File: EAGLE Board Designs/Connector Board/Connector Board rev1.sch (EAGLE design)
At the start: 39 parts, among them J1 CONNECTOR-8_μF_T_V_BLACK, J10 CONNECTOR-16_MF_T_V_, J11 CONNECTOR-18_MF_T_V_, J12 CONNECTOR-8_μF_T_V_BLACK, J2 CONNECTOR-8_μF_T_V_BLACK, J3 CONNECTOR-8_μF_T_V_BLACK, J4 CONNECTOR-10_MF_T_V_, J5 CONNECTOR-4_μF_T_V_BLACK, J6 CONNECTOR-34__, J7 CONNECTOR-34__, J8 CONNECTOR-4_μF_T_V_BLACK, J9 CONNECTOR-4_μF_T_V_BLACK, Q1 TRANSISTOR_N_MOS__DMG3406L-7, Q2 TRANSISTOR_P_MOS_SOT-23_DMP30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, Q3 TRANSISTOR_N_MOS__DMG3406L-7, Q4 TRANSISTOR_P_MOS_SOT-23_DMP30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, Q5 TRANSISTOR_N_MOS__DMG3406L-7, Q6 TRANSISTOR_P_MOS_SOT-23_DMP30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

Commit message: added CAN test points
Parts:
- added TP1, TP2, TP3, TP4, TP5, TP6: TEST_POINT, HyTechDevices:TEST_POINT
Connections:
- net CANH_1: now also TP3.1
- net CANH_2: now also TP1.1
- net CANH_3: now also TP6.1
- net CANL_1: now also TP4.1
- net CANL_2: now also TP2.1
- net CANL_3: now also TP5.1
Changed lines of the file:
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@@
 <part name="R2" library="HyTechDevices" deviceset="RESISTOR_?_*" device="0603" technology="100"/>
 <part name="R3" library="HyTechDevices" deviceset="RESISTOR_?_*" device="0603" technology="100"/>
+<part name="TP1" library="HyTechDevices" deviceset="TEST_POINT" device=""/>
+<part name="TP2" library="HyTechDevices" deviceset="TEST_POINT" device=""/>
+<part name="TP3" library="HyTechDevices" deviceset="TEST_POINT" device=""/>
+<part name="TP4" library="HyTechDevices" deviceset="TEST_POINT" device=""/>
+<part name="TP5" library="HyTechDevices" deviceset="TEST_POINT" device=""/>
+<part name="TP6" library="HyTechDevices" deviceset="TEST_POINT" device=""/>
 </parts>
 <sheets>
@@
 <attribute name="RESISTANCE" x="102.87" y="184.15" size="1.27" layer="96" align="top-center"/>
 </instance>
+<instance part="TP1" gate="G$1" x="254" y="198.12" smashed="yes" rot="R180">
+<attribute name="NAME" x="256.54" y="196.342" size="1.27" layer="95" rot="R180"/>
+<attribute name="MPN" x="256.54" y="199.898" size="1.27" layer="95" rot="R180" align="top-left"/>
+</instance>
+<instance part="TP2" gate="G$1" x="261.62" y="195.58" smashed="yes" rot="R180">
+<attribute name="NAME" x="264.16" y="193.802" size="1.27" layer="95" rot="R180"/>
+<attribute name="MPN" x="264.16" y="197.358" size="1.27" layer="95" rot="R180" align="top-left"/>
+</instance>
+<instance part="TP3" gate="G$1" x="269.24" y="193.04" smashed="yes" rot="R180">
+<attribute name="NAME" x="271.78" y="191.262" size="1.27" layer="95" rot="R180"/>
+<attribute name="MPN" x="271.78" y="194.818" size="1.27" layer="95" rot="R180" align="top-left"/>
+</instance>
+<instance part="TP4" gate="G$1" x="254" y="190.5" smashed="yes" rot="R180">
+<attribute name="NAME" x="256.54" y="188.722" size="1.27" layer="95" rot="R180"/>
+<attribute name="MPN" x="256.54" y="192.278" size="1.27" layer="95" rot="R180" align="top-left"/>
+</instance>
+<instance part="TP5" gate="G$1" x="261.62" y="187.96" smashed="yes" rot="R180">
+<attribute name="NAME" x="264.16" y="186.182" size="1.27" layer="95" rot="R180"/>
+<attribute name="MPN" x="264.16" y="189.738" size="1.27" layer="95" rot="R180" align="top-left"/>
+</instance>
+<instance part="TP6" gate="G$1" x="269.24" y="185.42" smashed="yes" rot="R180">
+<attribute name="NAME" x="271.78" y="183.642" size="1.27" layer="95" rot="R180"/>
+<attribute name="MPN" x="271.78" y="187.198" size="1.27" layer="95" rot="R180" align="top-left"/>
+</instance>
 </instances>
 <busses>
@@
 </segment>
 <segment>
-<wire x1="231.14" y1="187.96" x2="238.76" y2="187.96" width="0.1524" layer="91"/>
 <label x="238.76" y="187.96" size="1.27" layer="95" xref="yes"/>
 <pinref part="J10" gate="G$1" pin="5"/>
+<pinref part="TP5" gate="G$1" pin="1"/>
+<wire x1="231.14" y1="187.96" x2="259.08" y2="187.96" width="0.1524" layer="91"/>
 </segment>
 </net>
@@
 </segment>
 <segment>
-<wire x1="231.14" y1="185.42" x2="238.76" y2="185.42" width="0.1524" layer="91"/>
 <label x="238.76" y="185.42" size="1.27" layer="95" xref="yes"/>
 <pinref part="J10" gate="G$1" pin="6"/>
+<pinref part="TP6" gate="G$1" pin="1"/>
+<wire x1="231.14" y1="185.42" x2="266.7" y2="185.42" width="0.1524" layer="91"/>
 </segment>
 </net>
@@
 </segment>
 <segment>
-<wire x1="231.14" y1="195.58" x2="238.76" y2="195.58" width="0.1524" layer="91"/>
 <label x="238.76" y="195.58" size="1.27" layer="95" xref="yes"/>
 <pinref part="J10" gate="G$1" pin="2"/>
+<pinref part="TP2" gate="G$1" pin="1"/>
+<wire x1="231.14" y1="195.58" x2="259.08" y2="195.58" width="0.1524" layer="91"/>
 </segment>
 </net>
@@
 </segment>
 <segment>
-<wire x1="231.14" y1="198.12" x2="238.76" y2="198.12" width="0.1524" layer="91"/>
 <label x="238.76" y="198.12" size="1.27" layer="95" xref="yes"/>
 <pinref part="J10" gate="G$1" pin="1"/>
+<pinref part="TP1" gate="G$1" pin="1"/>
+<wire x1="231.14" y1="198.12" x2="251.46" y2="198.12" width="0.1524" layer="91"/>
 </segment>
 </net>
@@
 </segment>
 <segment>
-<wire x1="231.14" y1="190.5" x2="238.76" y2="190.5" width="0.1524" layer="91"/>
 <label x="238.76" y="190.5" size="1.27" layer="95" xref="yes"/>
 <pinref part="J10" gate="G$1" pin="4"/>
+<pinref part="TP4" gate="G$1" pin="1"/>
+<wire x1="231.14" y1="190.5" x2="251.46" y2="190.5" width="0.1524" layer="91"/>
 </segment>
 </net>
@@
 </segment>
 <segment>
-<wire x1="231.14" y1="193.04" x2="238.76" y2="193.04" width="0.1524" layer="91"/>
 <label x="238.76" y="193.04" size="1.27" layer="95" xref="yes"/>
 <pinref part="J10" gate="G$1" pin="3"/>
-</segment>
-</net>
+<pinref part="TP3" gate="G$1" pin="1"/>
+<wire x1="231.14" y1="193.04" x2="266.7" y2="193.04" width="0.1524" layer="91"/>
+</segment>
+</net>

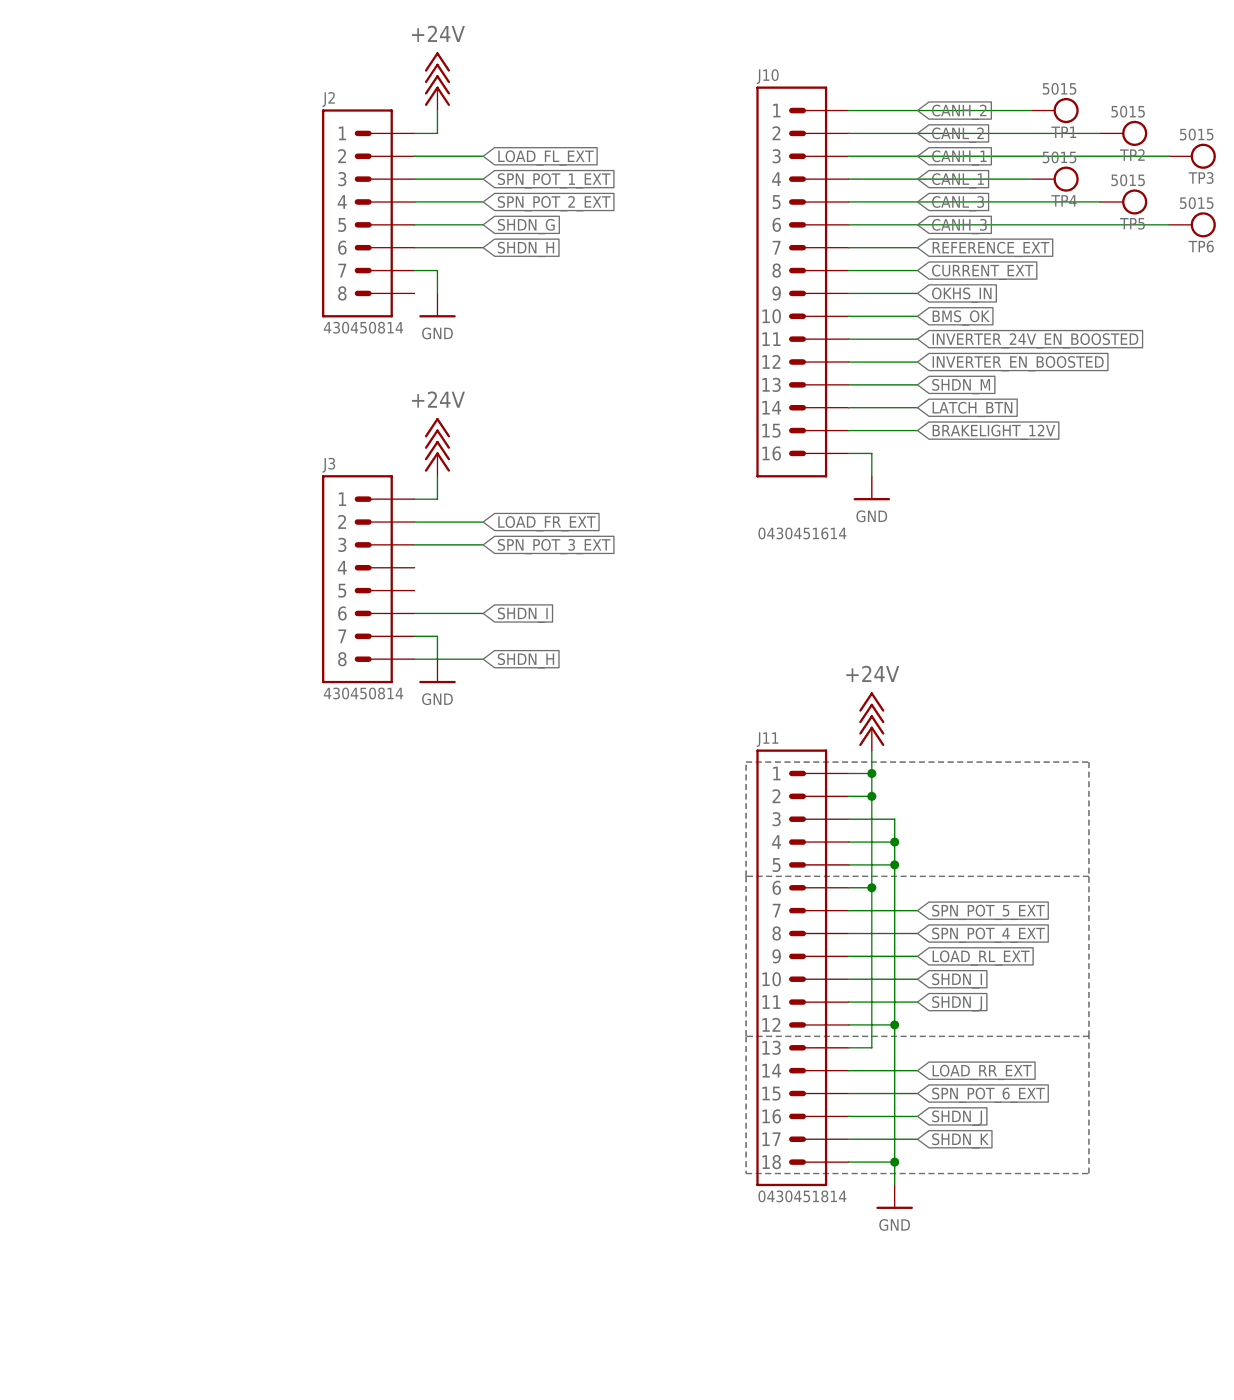
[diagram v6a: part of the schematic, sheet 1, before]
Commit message: moved test points
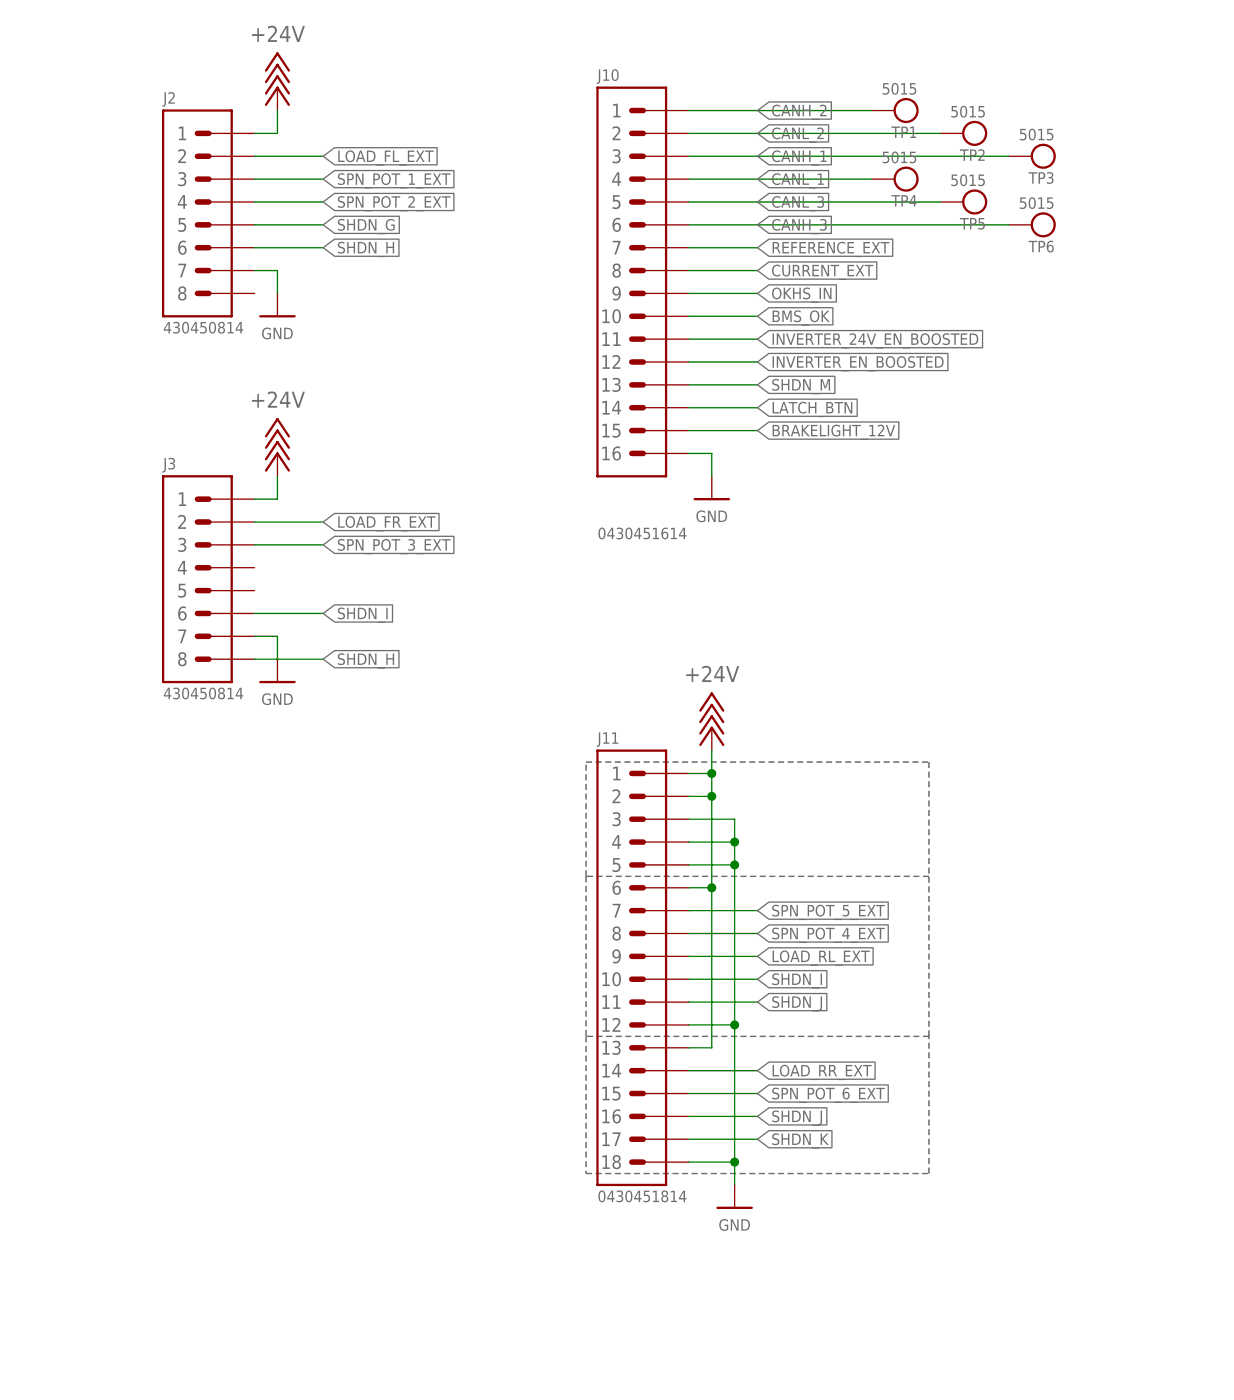
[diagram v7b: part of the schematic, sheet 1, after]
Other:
- moved on the sheet: J10, J11, J2, J3, TP1, TP2, TP3, TP4, TP5, TP6
